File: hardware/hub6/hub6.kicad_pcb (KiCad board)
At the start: 4 copper layers, 50.8 x 49.4 mm, 10 parts, among them J1 plate 1, J2 plate 2, J3 plate 3, J4 plate 4, J5 plate 5, J6 base, J7 XIAO D0-D6, J8 XIAO D7-5V, X1 XIAO

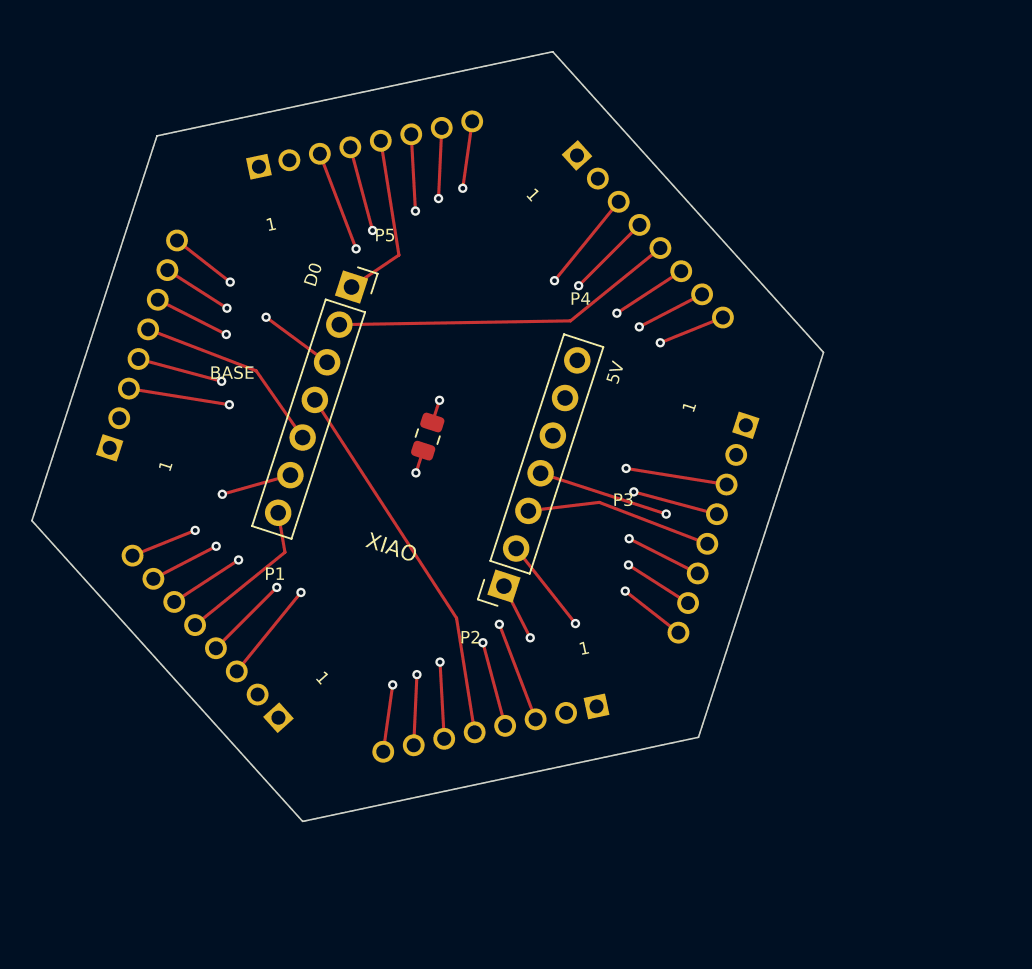
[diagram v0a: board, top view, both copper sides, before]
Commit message: hub6: add the 74HC138 back and widen the board to 25 mm to the edge
The cup's inside (measured from lcd_cup.stl) allows a hexagon 25 mm from
centre to edge when the board sits about 22 mm up, so the board grows from
22.5 mm and the 74HC138 goes under the XIAO again. A0, A1, A2 take D7, D8,
D9 and the six chip selects come from the decoder: U1's outputs run on In2
inside radius 12.4 mm through the gaps between socket pads, then up to F.Cu
at a lane via per header. assign.py now plans this (visibility graph on
In2) and writes layout.json, which make.py and the README follow. D3, D6
and D10 are free. ERC, DRC with schematic parity, and 14 tests pass.

Claude-Session: https://claude.ai/code/session_01WVeYczw2dnncq6csD58pZW
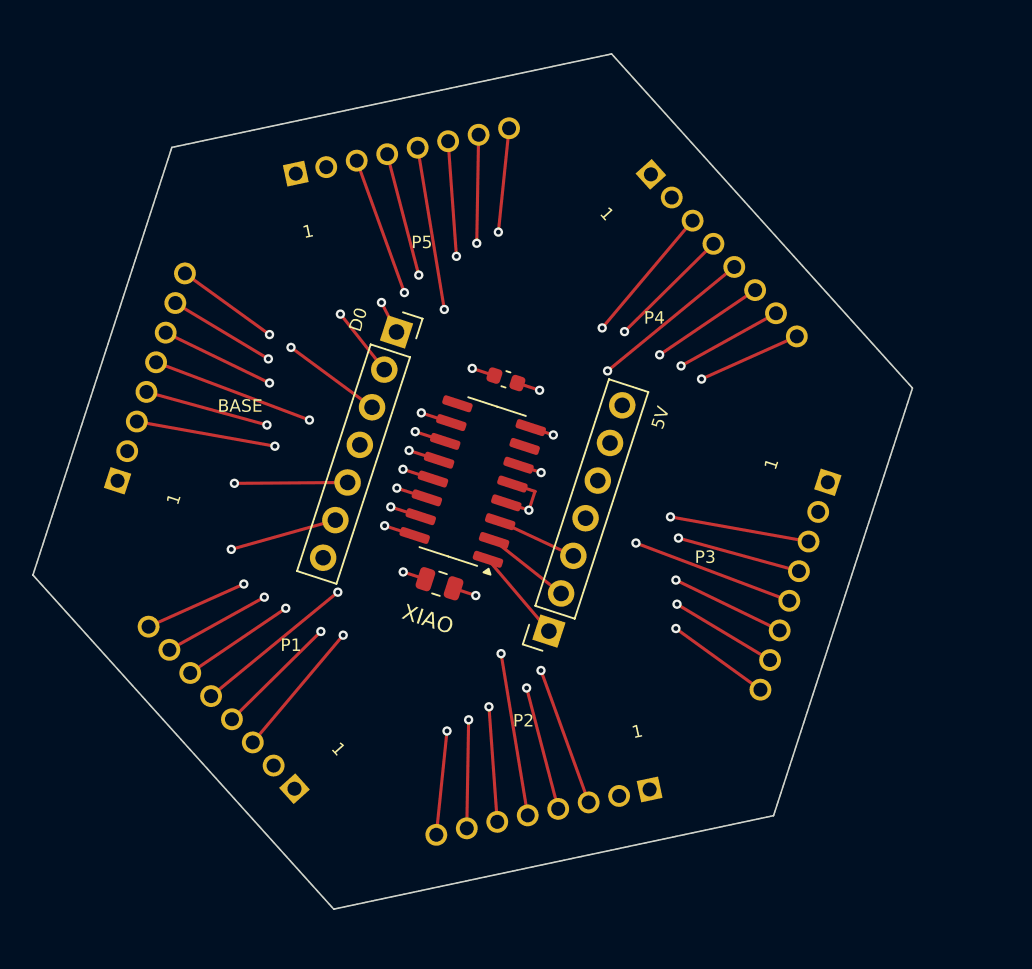
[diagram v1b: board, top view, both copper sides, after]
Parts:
- added C3: 100nF, Capacitor_SMD:C_0603_1608Metric, F.Cu at (131.0, 122.3)
- added U1: 74HC138, Package_SO:SOIC-16_3.9x9.9mm_P1.27mm, F.Cu at (128.9, 128.9)
- moved C2 9.48 mm to (126.7, 135.4), turned to 162 degrees
- moved J3 6.41 mm to (149.5, 135.6)
- moved J2 6.33 mm to (133.4, 150.1)
- moved J4 4.90 mm to (145.0, 114.3)
- moved J1 4.67 mm to (112.7, 143.4)
- moved J7 4.08 mm to (124.0, 119.3)
- moved X1 4.08 mm to (128.9, 128.9)
- moved J8 4.08 mm to (133.8, 138.5)
- moved J5 2.41 mm to (124.4, 107.6)
- moved J6 2.17 mm to (108.2, 122.2)
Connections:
- J7 pad 1: LCD_CS4 -> LCD_DIN
- J7 pad 2: LCD_CS3 -> LCD_CLK
- J7 pad 3: LCD_DIN -> LCD_DC
- J7 pad 4: LCD_CS1 -> unconnected-(J7-Pad4)
- J7 pad 5: LCD_CS5 -> LCD_RST
- J7 pad 6: LCD_CLK -> LCD_BL
- J7 pad 7: LCD_CS0 -> unconnected-(J7-Pad7)
- J8 pad 1: LCD_DC -> LCD_A0
- J8 pad 2: LCD_RST -> LCD_A1
- J8 pad 3: LCD_CS2 -> LCD_A2
- J8 pad 4: LCD_BL -> unconnected-(J8-Pad4)
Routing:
- net LCD_DC: track 124.4 -> 142.0 mm
- net LCD_CS2: track 12.0 -> 28.3 mm, vias 0 -> 2
- net LCD_RST: track 129.5 -> 145.2 mm
- net LCD_CLK: track 123.8 -> 138.8 mm
- net LCD_BL: track 135.6 -> 148.3 mm
- net LCD_DIN: track 125.1 -> 137.2 mm
- net LCD_CS0: track 10.00 -> 19.0 mm, vias 0 -> 2
- net LCD_CS4: track 11.1 -> 19.4 mm, vias 0 -> 2
- net GND: track 1.50 -> 8.85 mm, vias 1 -> 4
- net LCD_CS5: track 12.6 -> 19.4 mm, vias 0 -> 2
- net LCD_A0: track 0.00 -> 6.05 mm
- net LCD_A1: track 0.00 -> 5.49 mm
- net LCD_A2: track 0.00 -> 5.18 mm
- net +3V3: track 1.50 -> 6.55 mm, vias 1 -> 4
- net LCD_CS3: track 22.3 -> 26.3 mm, vias 0 -> 2
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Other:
- board size 50.8 x 49.4 mm -> 56.5 x 54.9 mm

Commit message: hub6: pentagon board with the display cables soldered straight in
The board becomes a regular pentagon (26 mm to the edge) whose edges face
the cup's five side plates one to one, instead of a hexagon whose corners
came close to the wall. The PH2.0 headers go: the cables (PH2.0 at the
display, bare 26 AWG wire here) are cut to length and soldered into rows
of eight holes, so no short double-ended cable has to be bought or crimped.
The side displays' rows run along the edges with two slots each for a
cable tie; the base display's row runs just outside the XIAO's right
socket row, over its plug, so its cable comes straight up from below and
no second board is needed.

The shared signals move to D0, D1, D3, D4, D5, level with the base row's
pins 3, 4, 6, 7, 8, and reach the rings (now 17.6 to 20.8 mm) through it.
assign.py now chooses the ring order (4 of 120 clear the stubs) and the
chip-select lanes for the new geometry. ERC, DRC and 17 tests pass.
fab.py also copies the upload files into fab6/.

Claude-Session: https://claude.ai/code/session_01WVeYczw2dnncq6csD58pZW
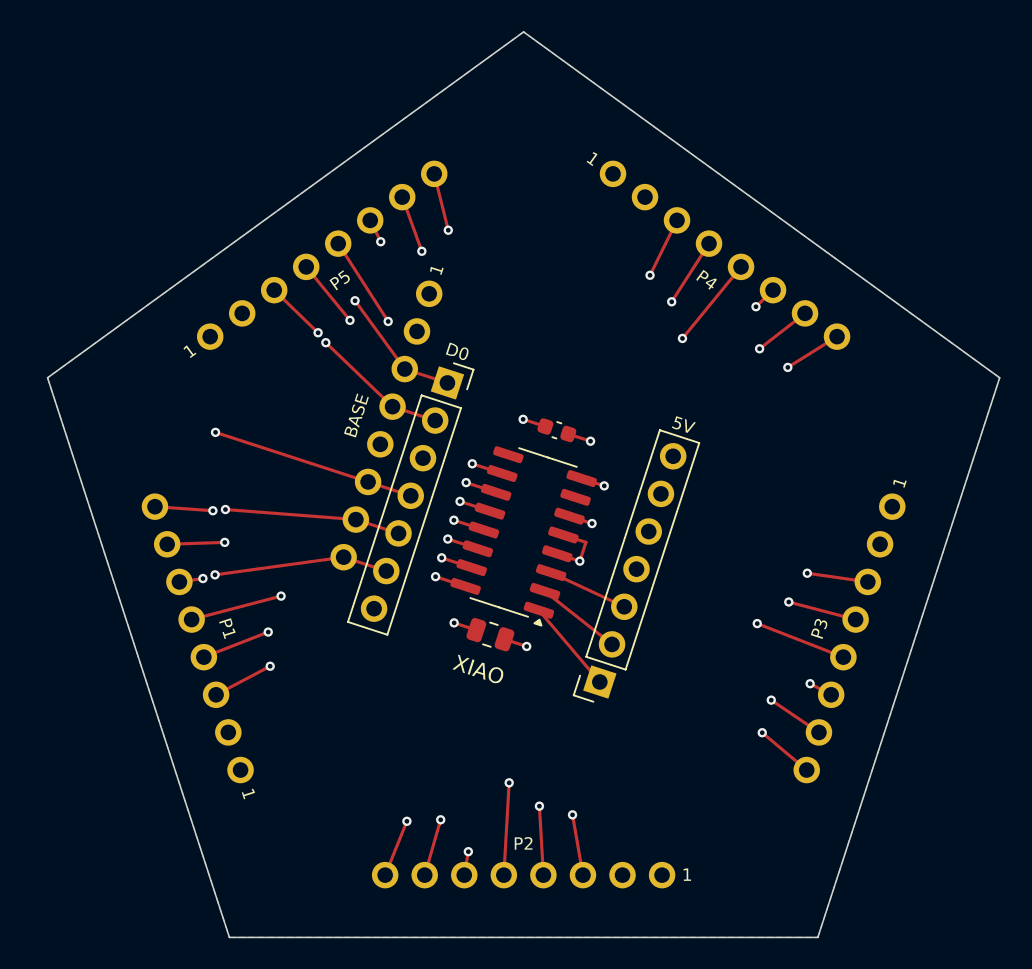
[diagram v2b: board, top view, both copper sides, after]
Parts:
- J1, J2, J3, J4, J5: footprint dodecahedron-earth:PH2.0_8P_Vertical_THT_C157974 -> dodecahedron-earth:Wire_1x08_P2.54_Tie
- J6: footprint dodecahedron-earth:PH2.0_8P_Vertical_THT_C157974 -> dodecahedron-earth:Wire_1x08_P2.54
- moved J6 15.4 mm to (123.3, 125.3), turned to 72 degrees
- moved J5 8.45 mm to (119.2, 114.3), turned to -144 degrees
- moved J3 4.89 mm to (153.1, 138.9)
- moved J1 4.71 mm to (111.2, 138.9), turned to -72 degrees
- moved J8 4.62 mm to (137.0, 141.7)
- moved C3 4.62 mm to (134.3, 125.6)
- moved C2 4.62 mm to (130.0, 138.7)
- moved J7 4.62 mm to (127.2, 122.5)
- moved U1 4.62 mm to (132.1, 132.1)
- moved X1 4.62 mm to (132.1, 132.1)
- moved J2 4.23 mm to (132.1, 154.1), turned to 0 degrees
- moved J4 0.08 mm to (145.1, 114.3), turned to 144 degrees
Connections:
- J7 pad 3: LCD_DC -> unconnected-(J7-Pad3)
- J7 pad 4: unconnected-(J7-Pad4) -> LCD_DC
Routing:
- net LCD_CS5: track 19.4 -> 8.29 mm, vias 2 -> 1
- net LCD_DC: track 142.0 -> 151.5 mm, vias 7 -> 6
- net LCD_BL: track 148.3 -> 155.5 mm, vias 7 -> 6
- net LCD_DIN: track 137.2 -> 143.5 mm, vias 7 -> 6
- net LCD_RST: track 145.2 -> 150.4 mm, vias 7 -> 6
- net LCD_CLK: track 138.8 -> 141.6 mm, vias 7 -> 6
- net LCD_CS1: track 25.1 -> 24.1 mm
- net LCD_CS3: track 26.3 -> 25.7 mm
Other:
- board size 56.5 x 54.9 mm -> 61.1 x 58.1 mm
- board text added: "J6 base (from below)"
- board text added: "hub6 rev B"
- board text removed: "J6 base"
- board text removed: "hub6 rev A"

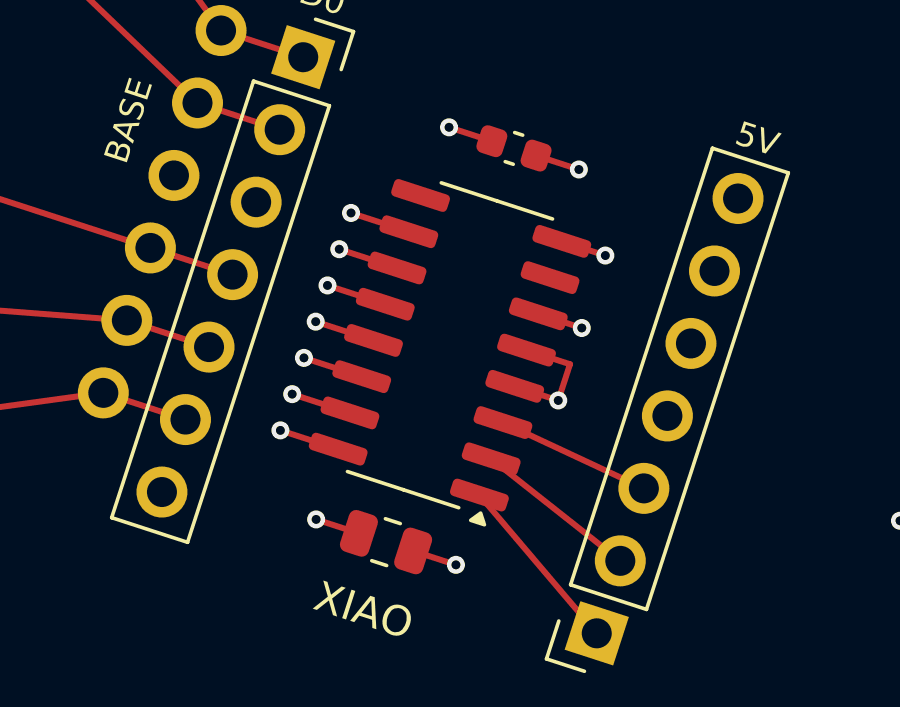
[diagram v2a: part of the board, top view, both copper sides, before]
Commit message: hub6: regenerate with the KiCad 10 footprint libraries, refresh fab6
The KiCad libraries went from 7.0 to 10.0 today, and DRC flagged the five library
footprints on the board (C2, C3, J7, J8, U1) as differing from the library. make.py
loaded them again: the pads, the 757 tracks and the filled zones are the same as before
(compared with the old board beside its own .kicad_pro); the courtyards, fab and silk
outlines and the 3D model paths are the new ones. ERC and DRC clean, 17 tests pass,
BOM and CPL unchanged.

Claude-Session: https://claude.ai/code/session_01WVeYczw2dnncq6csD58pZW
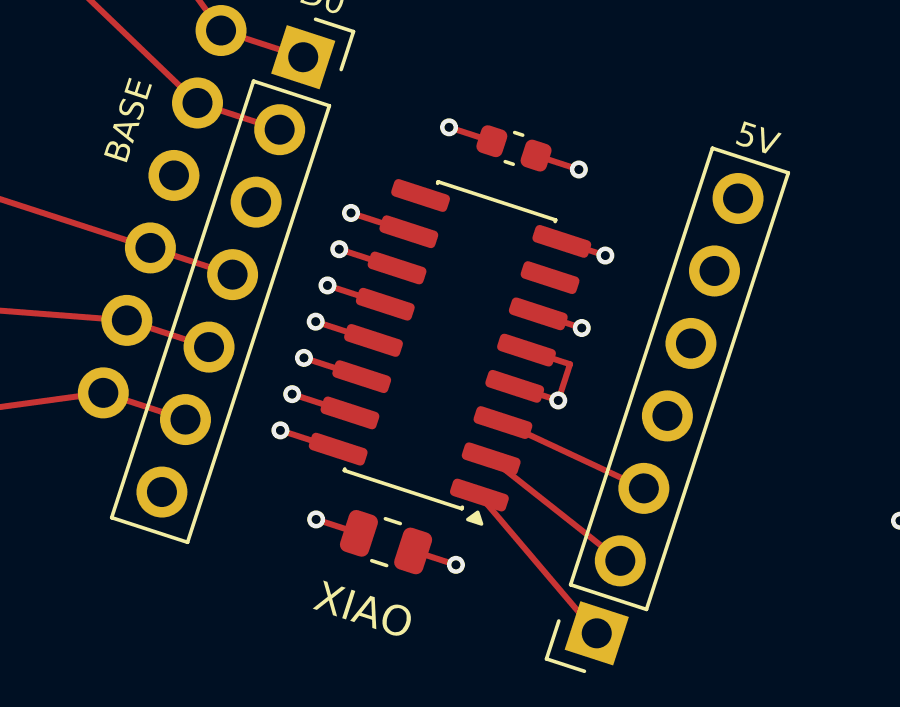
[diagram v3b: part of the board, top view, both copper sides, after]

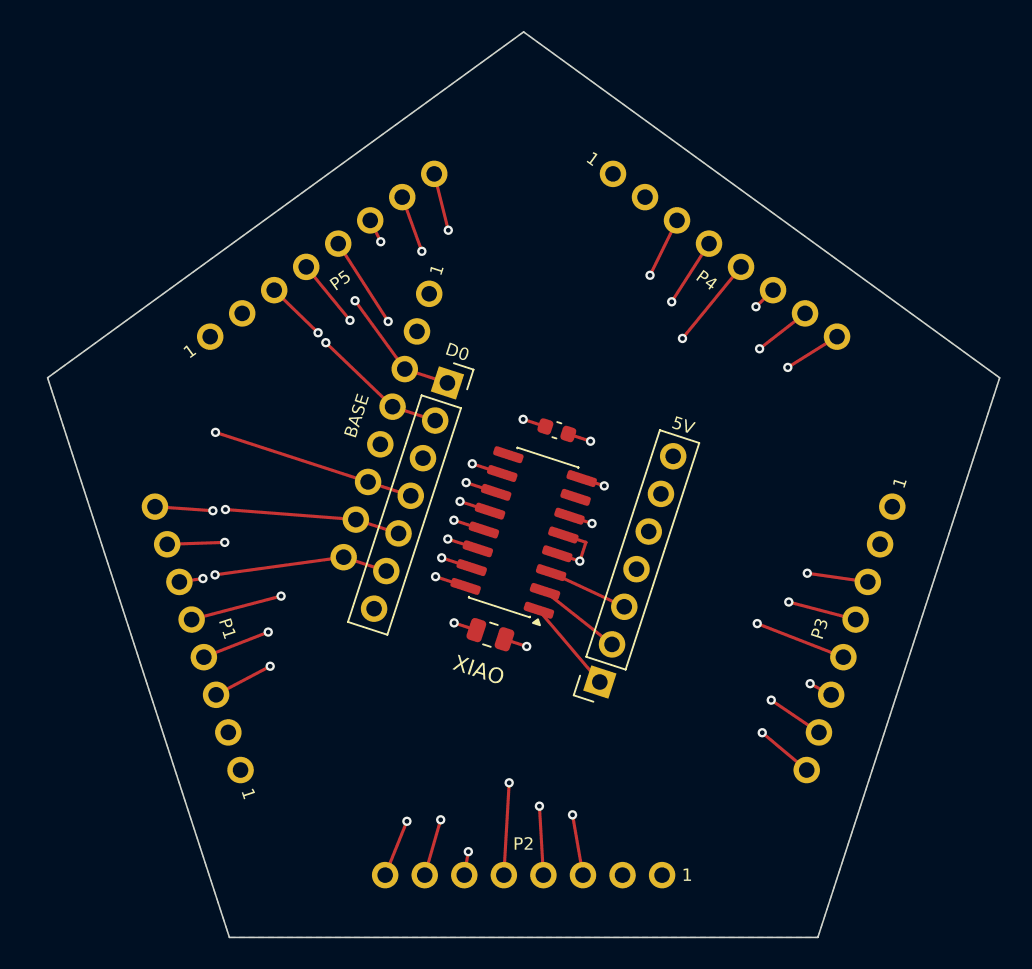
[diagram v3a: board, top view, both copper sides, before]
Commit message: hub6 rev C, board A: two layers, the XIAO moved to a board of its own
With the XIAO and its sockets gone from the middle, two layers carry everything: B.Cu
has only the rings (3V3 innermost, then the five shared signals) and GND round them;
F.Cu has straight lines that cross the rings freely. The side rows reach the rings by
radial stubs; J7 (a 2x5 header underneath, to board B) and the base display's holes
(now a 2x4 block, numbered like a DIP-8, over the base plug) reach them through two
of the pentagon's corners. The chip selects run in to the 74HC138 at the centre,
each to the output that lets no line cross another (P1 Y2, P2 Y1, P3 Y0, P4 Y5,
P5 Y4, base Y3). assign.py and layout.json are gone: nothing is left to search.
ERC and DRC clean, 14 tests. README still describes rev B; it follows with board B.

Claude-Session: https://claude.ai/code/session_01WVeYczw2dnncq6csD58pZW
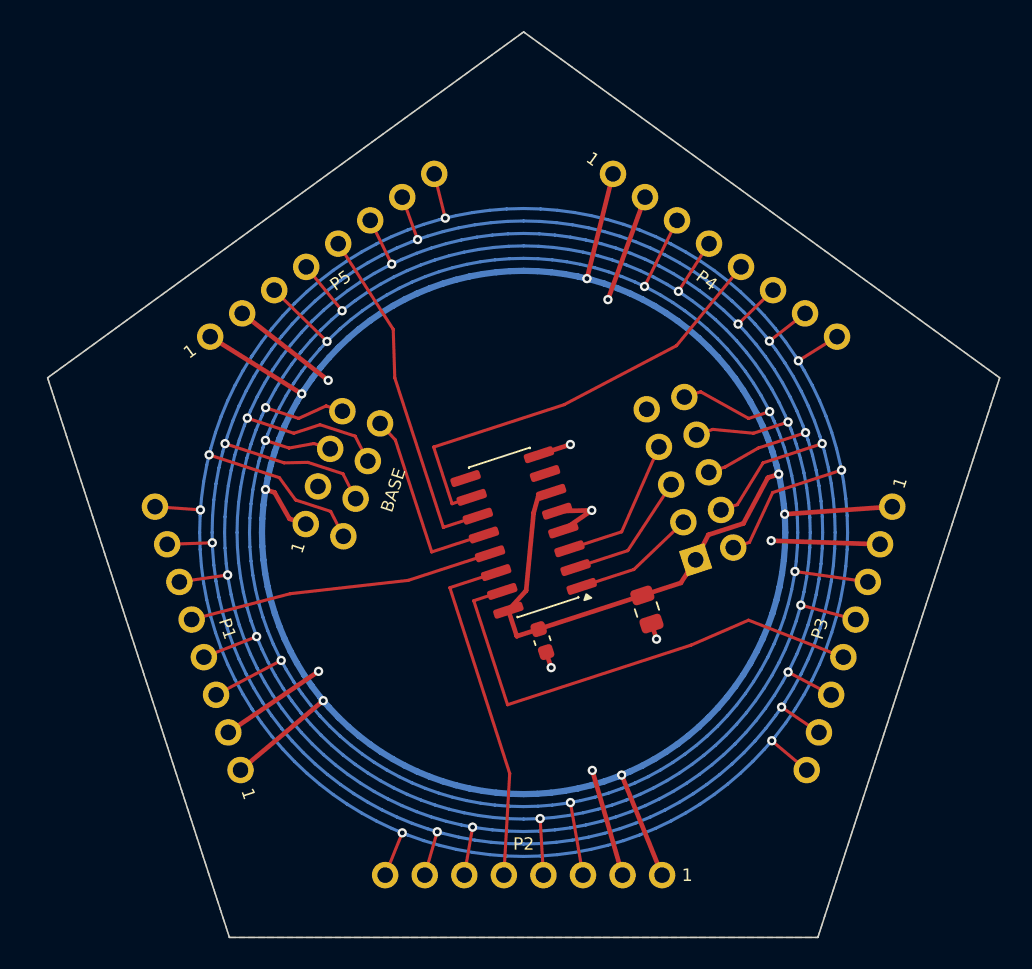
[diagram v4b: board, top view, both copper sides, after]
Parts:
- removed J8: XIAO D7-5V, Connector_PinSocket_2.54mm:PinSocket_1x07_P2.54mm_Vertical
- removed X1: XIAO, dodecahedron-earth:XIAO_ESP32S3_Outline
- J6: footprint dodecahedron-earth:Wire_1x08_P2.54 -> dodecahedron-earth:Wire_2x04_P2.54
- J7: value XIAO D0-D6 -> to board B; footprint Connector_PinSocket_2.54mm:PinSocket_1x07_P2.54mm_Vertical -> Connector_PinHeader_2.54mm:PinHeader_2x05_P2.54mm_Vertical; moved to B.Cu
- moved J7 19.6 mm to (143.2, 133.9), turned to 18 degrees
- moved C3 13.5 mm to (133.3, 139.1), turned to -72 degrees
- moved C2 10.2 mm to (140.1, 137.1), turned to -72 degrees
- moved J6 4.17 mm to (120.5, 128.4)
- turned U1 to -162 degrees
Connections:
- J7 pad 1: LCD_DIN -> +3V3
- J7 pad 2: LCD_CLK -> LCD_BL
- J7 pad 3: unconnected-(J7-Pad3) -> LCD_A0
- J7 pad 4: LCD_DC -> LCD_RST
- J7 pad 5: LCD_RST -> LCD_A1
- J7 pad 6: LCD_BL -> LCD_DC
- J7 pad 7: unconnected-(J7-Pad7) -> LCD_A2
- U1 pad 10: LCD_CS4 -> LCD_CS3
- U1 pad 11: LCD_CS5 -> LCD_CS4
- U1 pad 12: LCD_CS3 -> LCD_CS5
- U1 pad 13: LCD_CS2 -> LCD_CS0
- U1 pad 15: LCD_CS0 -> LCD_CS2
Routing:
- net +3V3: track 6.55 -> 175.3 mm, vias 4 -> 7
- net GND: track 8.85 -> 43.7 mm, vias 4 -> 9
- net LCD_BL: track 155.5 -> 165.3 mm, vias 6 -> 7
- net LCD_RST: track 150.4 -> 158.1 mm, vias 6 -> 7
- net LCD_A2: track 5.18 -> 9.48 mm
- net LCD_CS5: track 8.29 -> 12.5 mm, vias 1 -> 0
- net LCD_CLK: track 141.6 -> 145.1 mm, vias 6 -> 7
- net LCD_CS2: track 28.6 -> 31.9 mm, vias 2 -> 0
- net LCD_A1: track 5.49 -> 8.60 mm
- net LCD_CS3: track 25.7 -> 28.6 mm, vias 2 -> 0
- net LCD_CS4: track 19.6 -> 22.1 mm, vias 2 -> 0
- net LCD_CS1: track 24.1 -> 22.2 mm, vias 2 -> 0
- net LCD_A0: track 6.05 -> 7.92 mm
- net LCD_DIN: track 143.5 -> 144.6 mm, vias 6 -> 7
- net LCD_CS0: track 18.8 -> 19.7 mm, vias 2 -> 0
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- added copper zone on B.Cu, net GND
- added copper zone on F.Cu, net GND
- removed copper zone on B.Cu, net +3V3
- removed copper zone on In1.Cu, net GND
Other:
- copper layers 4 -> 2
- board text added: "J7 to board B"
- board text added: "hub6 rev C"
- board text removed: "hub6 rev B"
